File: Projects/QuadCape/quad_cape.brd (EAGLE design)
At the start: 71.8 x 54.6 mm, 9 parts, among them U1 ADXL345, U2 ITG-3200, U3 LS20031, U4 ATMEGA8U2AU

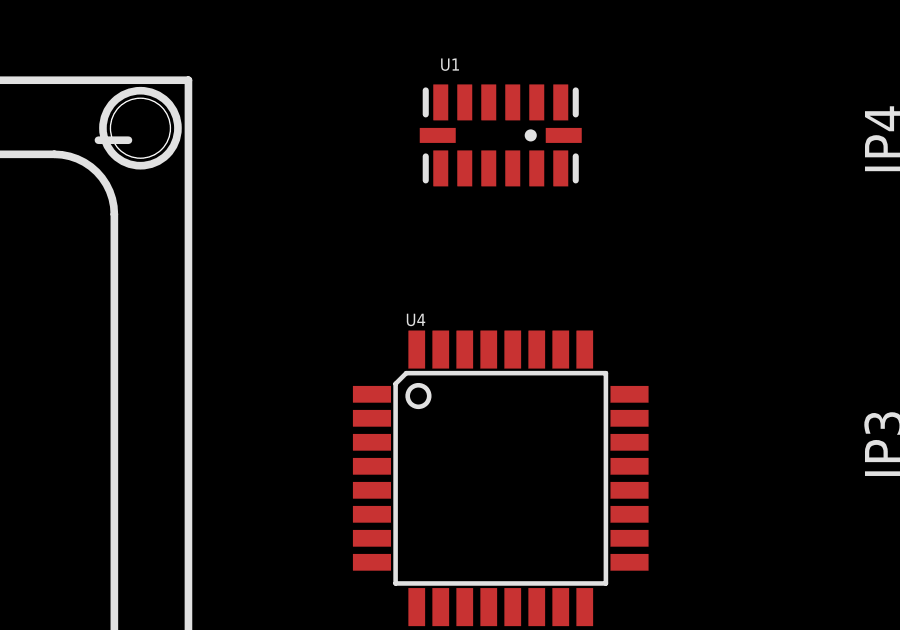
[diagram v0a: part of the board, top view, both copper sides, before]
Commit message: Began wiring up some connections
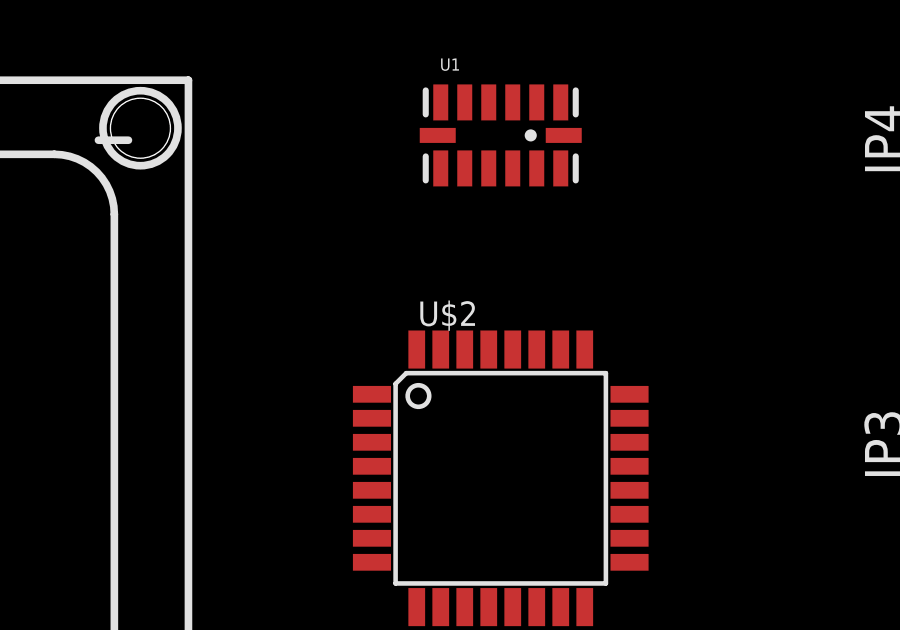
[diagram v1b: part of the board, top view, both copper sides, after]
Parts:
- removed U4: ATMEGA8U2AU, SparkFun-DigitalIC:TQFP32-08
- added U$2: ATMEGA328P-AU, custom:TQFP32-08
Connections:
- new net N$1: U$2.30, U3.3
- new net N$10: U$2.13
- new net N$2: U$2.31, U3.2
- new net N$3: U$1.75, U$2.16
- new net N$4: U$1.76, U$2.15
- new net N$5: U$2.14
- new net N$6: U$1.77, U$2.17
- new net N$7: U1.13, U2.24
- new net N$8: U$2.28, U1.14, U2.23
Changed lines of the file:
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@@
 <element name="JP3" library="adafruit" package="1X03" value="" x="78.74" y="33.02" rot="R90"/>
 <element name="JP4" library="adafruit" package="1X03" value="" x="78.74" y="43.18" rot="R90"/>
-<element name="U4" library="SparkFun-DigitalIC" package="TQFP32-08" value="ATMEGA8U2AU" x="63.5" y="29.21"/>
+<element name="U$2" library="custom" package="TQFP32-08" value="ATMEGA328P-AU" x="63.5" y="29.21" smashed="yes">
+<attribute name="NAME" x="60.7314" y="34.29" size="0.8128" layer="25"/>
+<attribute name="VALUE" x="59.2074" y="22.86" size="0.8128" layer="27"/>
+</element>
 </elements>
 <signals>
@@
 <contactref element="U3" pad="5"/>
 </signal>
+<signal name="N$1">
+<contactref element="U3" pad="3"/>
+<contactref element="U$2" pad="30"/>
+<wire x1="38.1" y1="21.11" x2="62.3" y2="33.5026" width="0" layer="19" extent="1-1"/>
+</signal>
+<signal name="N$2">
+<contactref element="U3" pad="2"/>
+<contactref element="U$2" pad="31"/>
+<wire x1="40.64" y1="21.11" x2="61.5" y2="33.5026" width="0" layer="19" extent="1-1"/>
+</signal>
+<signal name="N$3">
+<contactref element="U$1" pad="75"/>
+<contactref element="U$2" pad="16"/>
+<wire x1="54.61" y1="1.905" x2="66.3" y2="24.9174" width="0" layer="19" extent="1-1"/>
+</signal>
+<signal name="N$4">
+<contactref element="U$1" pad="76"/>
+<contactref element="U$2" pad="15"/>
+<wire x1="54.61" y1="4.445" x2="65.5" y2="24.9174" width="0" layer="19" extent="1-1"/>
+</signal>
+<signal name="N$6">
+<contactref element="U$2" pad="17"/>
+<contactref element="U$1" pad="77"/>
+<wire x1="57.15" y1="1.905" x2="67.7926" y2="26.41" width="0" layer="19" extent="1-1"/>
+</signal>
+<signal name="N$8">
+<contactref element="U$2" pad="28"/>
+<contactref element="U2" pad="23"/>
+<contactref element="U1" pad="14"/>
+<wire x1="63.9" y1="33.5026" x2="65.6" y2="40.64" width="0" layer="19" extent="1-1"/>
+<wire x1="62.75" y1="18.51" x2="63.9" y2="33.5026" width="0" layer="19" extent="1-1"/>
+</signal>
+<signal name="N$7">
+<contactref element="U2" pad="24"/>
+<contactref element="U1" pad="13"/>
+<wire x1="62.25" y1="18.51" x2="65.5" y2="39.54" width="0" layer="19" extent="1-1"/>
+</signal>
+<signal name="N$10">
+<contactref element="U$2" pad="13"/>
+</signal>
+<signal name="N$5">
+<contactref element="U$2" pad="14"/>
+</signal>
 </signals>

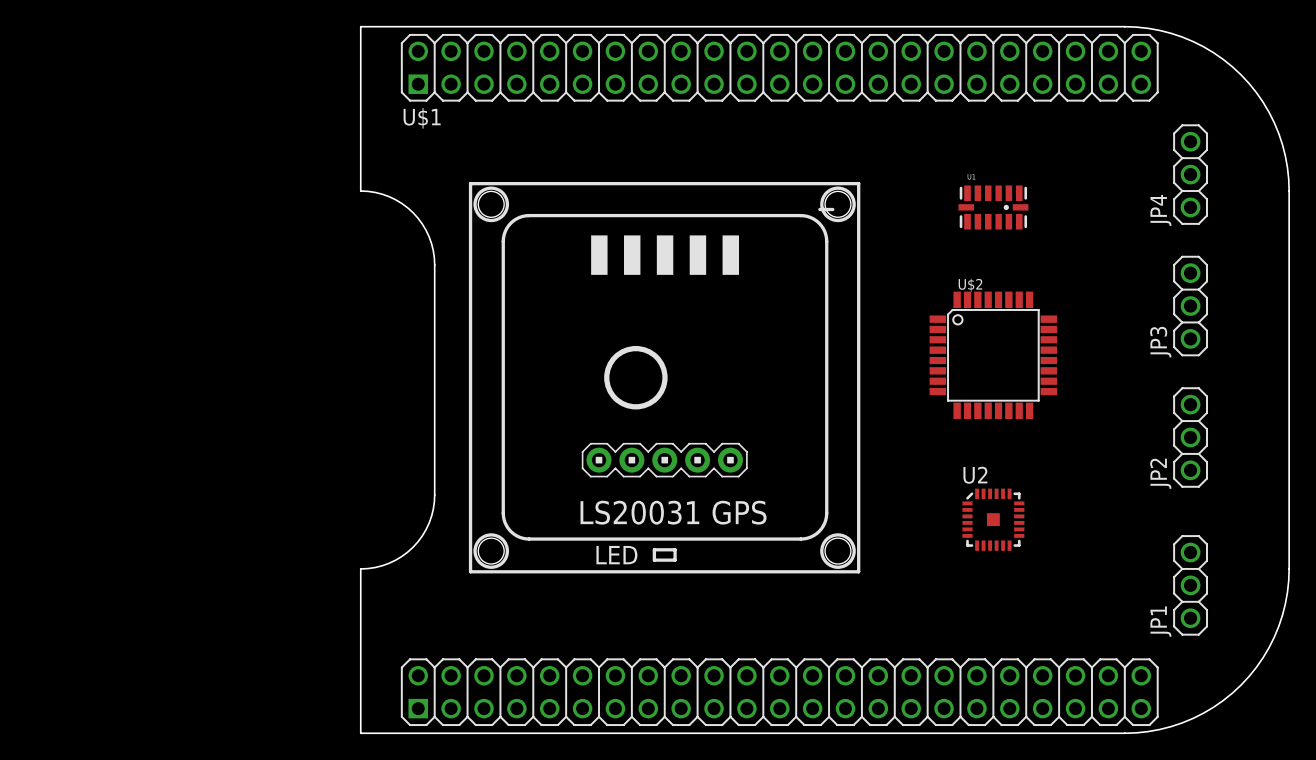
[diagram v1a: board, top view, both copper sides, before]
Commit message: Swapped symbol for Mega328 for a better on I had already made a while ago (oops)
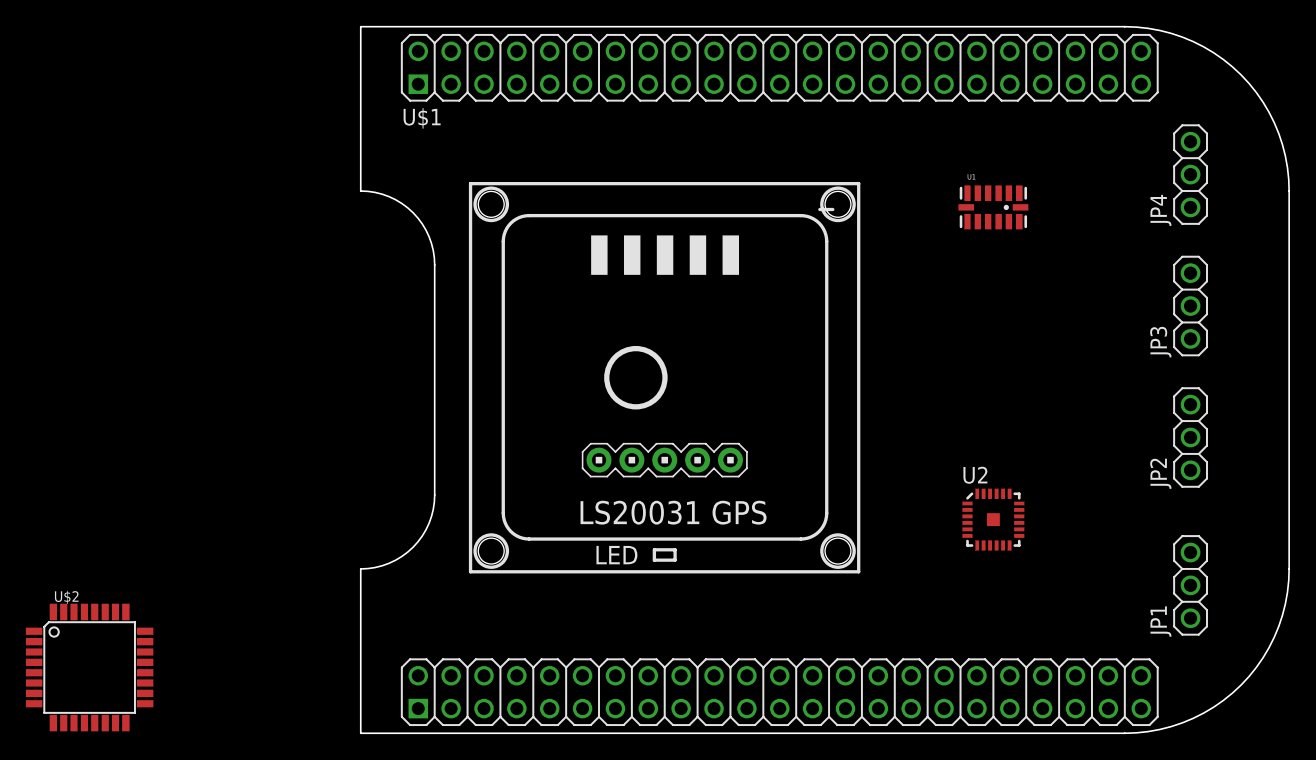
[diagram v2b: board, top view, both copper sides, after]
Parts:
- U$2: value ATMEGA328P-AU -> MEGA328P
- moved U$2 73.9 mm to (-6.35, 5.08)
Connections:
- removed net GND$1: U3.4
- removed net GND$2: U3.5
- removed net N$4 (its old number): U$1.76, U$2.15
- new net N$11: U$2.15
- new net N$12: U$2.1
- net GND: now also U$2.21, U$2.3, U$2.5, U3.4, U3.5
- net N$3: no longer U$2.16
- net N$6: no longer U$2.17
- net N$7: now also U$2.27
- net VCC: now also U$2.4, U$2.6
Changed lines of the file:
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@@
 <element name="JP3" library="adafruit" package="1X03" value="" x="78.74" y="33.02" rot="R90"/>
 <element name="JP4" library="adafruit" package="1X03" value="" x="78.74" y="43.18" rot="R90"/>
-<element name="U$2" library="custom" package="TQFP32-08" value="ATMEGA328P-AU" x="63.5" y="29.21" smashed="yes">
-<attribute name="NAME" x="60.7314" y="34.29" size="0.8128" layer="25"/>
-<attribute name="VALUE" x="59.2074" y="22.86" size="0.8128" layer="27"/>
-</element>
+<element name="U$2" library="custom" package="TQFP32-08" value="MEGA328P" x="-6.35" y="5.08"/>
 </elements>
 <signals>
@@
 <contactref element="U$1" pad="1"/>
 <contactref element="U$1" pad="2"/>
+<contactref element="U3" pad="4"/>
+<contactref element="U3" pad="5"/>
+<contactref element="U$2" pad="21"/>
+<contactref element="U$2" pad="3"/>
+<contactref element="U$2" pad="5"/>
 <wire x1="19.05" y1="50.165" x2="19.05" y2="52.705" width="0" layer="19" extent="1-1"/>
-<wire x1="19.05" y1="4.445" x2="19.05" y2="50.165" width="0" layer="19" extent="1-1"/>
+<wire x1="33.02" y1="21.11" x2="19.05" y2="50.165" width="0" layer="19" extent="1-1"/>
+<wire x1="35.56" y1="21.11" x2="33.02" y2="21.11" width="0" layer="19" extent="1-1"/>
+<wire x1="19.05" y1="4.445" x2="33.02" y2="21.11" width="0" layer="19" extent="1-1"/>
 <wire x1="19.05" y1="1.905" x2="19.05" y2="4.445" width="0" layer="19" extent="1-1"/>
+<wire x1="-2.0574" y1="5.48" x2="19.05" y2="4.445" width="0" layer="19" extent="1-1"/>
+<wire x1="-10.6426" y1="4.68" x2="-2.0574" y2="5.48" width="0" layer="19" extent="1-1"/>
+<wire x1="-10.6426" y1="6.28" x2="-10.6426" y2="4.68" width="0" layer="19" extent="1-1"/>
 </signal>
 <signal name="VDD_3V3EXP">
@@
 <signal name="VCC">
 <contactref element="U3" pad="1"/>
+<contactref element="U3" pad="1"/>
+<contactref element="U$2" pad="4"/>
+<contactref element="U$2" pad="6"/>
+<wire x1="-10.6426" y1="5.48" x2="43.18" y2="21.11" width="0" layer="19" extent="1-1"/>
+<wire x1="-10.6426" y1="3.88" x2="-10.6426" y2="5.48" width="0" layer="19" extent="1-1"/>
 </signal>
 <signal name="GND1">
@@
 <signal name="GND2">
 </signal>
-<signal name="GND$1">
-<contactref element="U3" pad="4"/>
-</signal>
-<signal name="GND$2">
-<contactref element="U3" pad="5"/>
-</signal>
 <signal name="N$1">
 <contactref element="U3" pad="3"/>
 <contactref element="U$2" pad="30"/>
-<wire x1="38.1" y1="21.11" x2="62.3" y2="33.5026" width="0" layer="19" extent="1-1"/>
+<wire x1="-7.55" y1="9.3726" x2="38.1" y2="21.11" width="0" layer="19" extent="1-1"/>
 </signal>
 <signal name="N$2">
 <contactref element="U3" pad="2"/>
 <contactref element="U$2" pad="31"/>
-<wire x1="40.64" y1="21.11" x2="61.5" y2="33.5026" width="0" layer="19" extent="1-1"/>
+<wire x1="-8.35" y1="9.3726" x2="40.64" y2="21.11" width="0" layer="19" extent="1-1"/>
 </signal>
 <signal name="N$3">
 <contactref element="U$1" pad="75"/>
-<contactref element="U$2" pad="16"/>
-<wire x1="54.61" y1="1.905" x2="66.3" y2="24.9174" width="0" layer="19" extent="1-1"/>
-</signal>
-<signal name="N$4">
-<contactref element="U$1" pad="76"/>
-<contactref element="U$2" pad="15"/>
-<wire x1="54.61" y1="4.445" x2="65.5" y2="24.9174" width="0" layer="19" extent="1-1"/>
 </signal>
 <signal name="N$6">
-<contactref element="U$2" pad="17"/>
 <contactref element="U$1" pad="77"/>
-<wire x1="57.15" y1="1.905" x2="67.7926" y2="26.41" width="0" layer="19" extent="1-1"/>
 </signal>
 <signal name="N$8">
-<contactref element="U$2" pad="28"/>
 <contactref element="U2" pad="23"/>
 <contactref element="U1" pad="14"/>
-<wire x1="63.9" y1="33.5026" x2="65.6" y2="40.64" width="0" layer="19" extent="1-1"/>
-<wire x1="62.75" y1="18.51" x2="63.9" y2="33.5026" width="0" layer="19" extent="1-1"/>
+<contactref element="U$2" pad="28"/>
+<wire x1="62.75" y1="18.51" x2="65.6" y2="40.64" width="0" layer="19" extent="1-1"/>
+<wire x1="-5.95" y1="9.3726" x2="62.75" y2="18.51" width="0" layer="19" extent="1-1"/>
 </signal>
 <signal name="N$7">
 <contactref element="U2" pad="24"/>
 <contactref element="U1" pad="13"/>
+<contactref element="U$2" pad="27"/>
 <wire x1="62.25" y1="18.51" x2="65.5" y2="39.54" width="0" layer="19" extent="1-1"/>
+<wire x1="-5.15" y1="9.3726" x2="62.25" y2="18.51" width="0" layer="19" extent="1-1"/>
 </signal>
-<signal name="N$10">
+<signal name="N$4">
 <contactref element="U$2" pad="13"/>
 </signal>
-<signal name="N$5">
+<signal name="N$9">
 <contactref element="U$2" pad="14"/>
 </signal>
+<signal name="N$11">
+<contactref element="U$2" pad="15"/>
+</signal>
+<signal name="N$12">
+<contactref element="U$2" pad="1"/>
+</signal>
 </signals>

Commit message: Sync
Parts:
- JP1, JP2, JP3, JP4: device adafruit:1X03 -> SparkFun-Connectors:1X04
- moved U$2 74.7 mm to (64.8, 27.9)
- moved JP4 36.8 mm to (78.7, 6.35)
- moved JP1 29.2 mm to (78.7, 40.6)
- moved JP3 15.2 mm to (78.7, 17.8)
- moved JP2 6.35 mm to (78.7, 29.2)
- moved U3 0.57 mm to (38.5, 27.1), turned to 270 degrees
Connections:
- new net +5V: JP1.1, JP2.1, JP3.1, JP4.1, U$1.52
- new net N$15: U$1.77, U$2.17
- new net N$5: JP3.2, U$2.10
- net GND: now also JP1.3, JP1.4, JP2.3, JP2.4, JP3.3, JP3.4, JP4.3, JP4.4, U$1.89, U$1.90, U$1.91, U$1.92, U1.2, U1.4, U1.5, U2.18, U3.1, U3.2; no longer U3.4, U3.5
- net N$1: now also U3.4; no longer U3.3
- net N$11: now also U$1.74; no longer U$2.15
- net N$12: now also JP4.2, U$2.9; no longer U$2.1
- net N$2: now also U3.3; no longer U3.2
- net N$3: now also U$2.15
- net N$4: now also JP2.2
- net N$6: now also U$1.76, U$2.16; no longer U$1.77
- net N$9: now also JP1.2
- net VCC: now also U3.5; no longer U3.1
- net VDD_5V: no longer U$1.52
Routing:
- net GND: track 0.00 -> 93.3 mm, vias 0 -> 3
- net +5V: track 0.00 -> 58.3 mm
- net N$15: track 0.00 -> 35.0 mm, vias 0 -> 1
- net N$3: track 0.00 -> 34.3 mm, vias 0 -> 3
- net N$5: track 0.00 -> 32.6 mm, vias 0 -> 1
- net N$8: track 0.00 -> 30.1 mm, vias 0 -> 4
- net N$6: track 0.00 -> 28.7 mm
- net N$1: track 0.00 -> 27.6 mm, vias 0 -> 2
- net N$9: track 0.00 -> 26.9 mm, vias 0 -> 2
- net N$7: track 0.00 -> 24.4 mm, vias 0 -> 2
- net N$12: track 0.00 -> 24.4 mm, vias 0 -> 2
- net VCC: track 0.00 -> 22.8 mm
- net N$2: track 0.00 -> 22.1 mm
- net N$4: track 0.00 -> 19.4 mm, vias 0 -> 2
- net VDD_3V3EXP: track 0.00 -> 2.54 mm
- added copper zone on layer 1, net GND

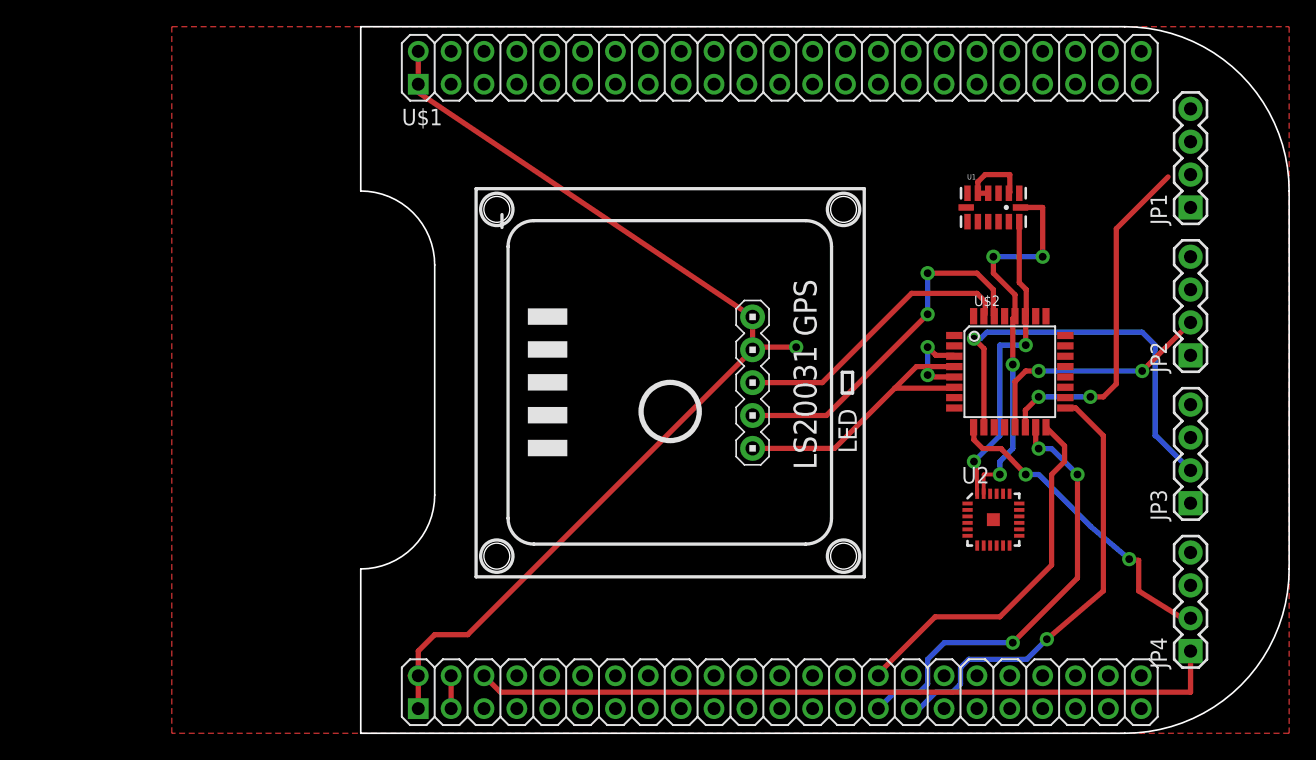
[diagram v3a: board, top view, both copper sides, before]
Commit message: Replaced individual Compass and Gyro with Sparkfun 6DOF-Digital module
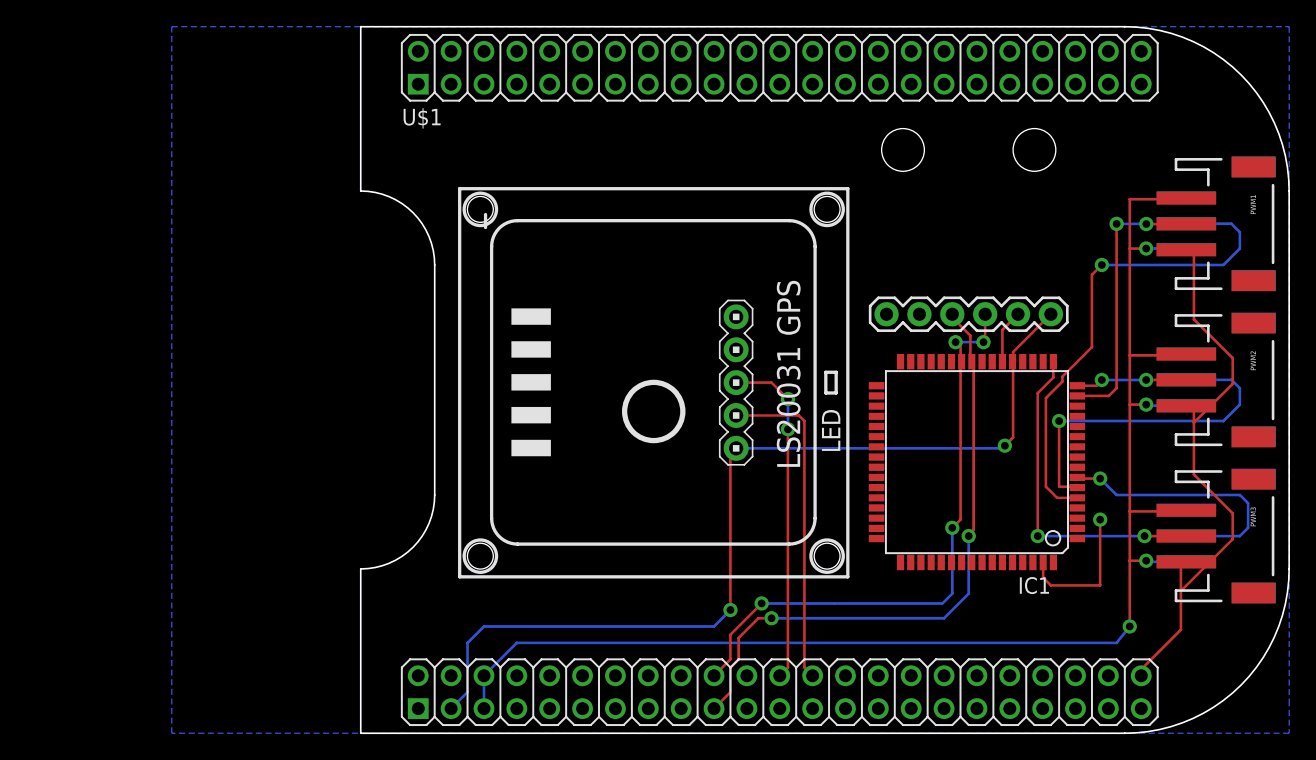
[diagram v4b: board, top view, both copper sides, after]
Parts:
- removed JP1, JP2, JP3, JP4: (no value), SparkFun-Connectors:1X04
- removed U1: ADXL345, SparkFun-Sensors:LGA14
- removed U2: ITG-3200, SparkFun-Sensors:QFN-24
- added IC1: MEGA64-A, avr:TQFP64
- added PWM1, PWM2, PWM3, PWM4, PWM5, PWM6: (no value), SparkFun-Connectors:JST-3-SMD
- U$2: value MEGA328P -> 6DOF-DIGITAL; device custom:TQFP32-08 -> SparkFun-Breakouts:6DOF_DIGITAL_V10
- moved U$2 22.5 mm to (54.0, 47.6), turned to 270 degrees
- moved U3 1.27 mm to (37.3, 27.1)
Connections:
- removed net N$1: U$2.30, U3.4
- removed net N$11: U$1.74
- removed net N$12: JP4.2, U$2.9
- removed net N$15: U$1.77, U$2.17
- removed net N$2: U$2.31, U3.3
- removed net N$3: U$1.75, U$2.15
- removed net N$4: JP2.2, U$2.13
- removed net N$5: JP3.2, U$2.10
- removed net N$6: U$1.76, U$2.16
- removed net N$7: U$2.27, U1.13, U2.24
- removed net N$8: U$2.28, U1.14, U2.23
- removed net N$9: JP1.2, U$2.14
- removed net VDD_3V3EXP: U$1.49, U$1.50
- removed net VDD_5V: U$1.51
- new net GND1: IC1.53
- new net PWM1: IC1.15, PWM1.2
- new net PWM2: IC1.16, PWM2.2
- new net PWM3: IC1.17, PWM3.2
- new net PWM4: IC1.5, PWM4.2
- new net PWM5: IC1.6, PWM5.2
- new net PWM6: IC1.7, PWM6.2
- new net RXD: U$1.72, U3.4
- new net SCL: IC1.25, U$1.65, U$2.4
- new net SDA: IC1.26, U$1.66, U$2.3
- new net TXD: U$1.70, U3.3
- new net VCC1: IC1.52
- new net VCCIO: U$1.50
- net +5V: now also PWM1.1, PWM2.1, PWM3.1, PWM4.1, PWM5.1, PWM6.1, U$1.51; no longer JP1.1, JP2.1, JP3.1, JP4.1
- net GND: now also IC1.22, IC1.63, PWM1.3, PWM2.3, PWM3.3, PWM4.3, PWM5.3, PWM6.3, U$2.2; no longer JP1.3, JP1.4, JP2.3, JP2.4, JP3.3, JP3.4, JP4.3, JP4.4, U$2.21, U$2.3, U$2.5, U1.2, U1.4, U1.5, U2.18
- net VCC: now also IC1.21, U$1.49, U$2.1; no longer U$2.4, U$2.6
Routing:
- net +5V: track 58.3 -> 116.2 mm, vias 0 -> 4
- net VCC: track 22.8 -> 73.1 mm, vias 0 -> 2
- net SCL: track 0.00 -> 47.9 mm, vias 0 -> 2
- net SDA: track 0.00 -> 46.6 mm, vias 0 -> 4
- net PWM4: track 0.00 -> 38.6 mm, vias 0 -> 1
- net N$15: track 35.0 -> 0.00 mm, vias 1 -> 0
- net GND: track 93.3 -> 59.1 mm, vias 3 -> 1
- net N$3: track 34.3 -> 0.00 mm, vias 3 -> 0
- net N$5: track 32.6 -> 0.00 mm, vias 1 -> 0
- net N$8: track 30.1 -> 0.00 mm, vias 4 -> 0
- net N$6: track 28.7 -> 0.00 mm
- net N$1: track 27.6 -> 0.00 mm, vias 2 -> 0
- net N$9: track 26.9 -> 0.00 mm, vias 2 -> 0
- net PWM5: track 0.00 -> 26.7 mm, vias 0 -> 1
- net TXD: track 0.00 -> 26.2 mm, vias 0 -> 2
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- added copper zone on layer 16, net GND
- removed copper zone on layer 1, net GND
